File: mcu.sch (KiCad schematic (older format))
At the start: 95 parts, among them J1 USB_B_Mini, J10 JTAG, J2 SPI1, J3 uSD, J4 I2C1, J5 serial1, J6 serial2, J9 EXT_IOS, SW1 reset, U1 LP38691SD-3.3, U2 USBLC6-2SC6, U3 AT25SF641, U4 BQ24190, U5 STM32F750Z8, Y1 25 MHz, Y2 32.768 kHz

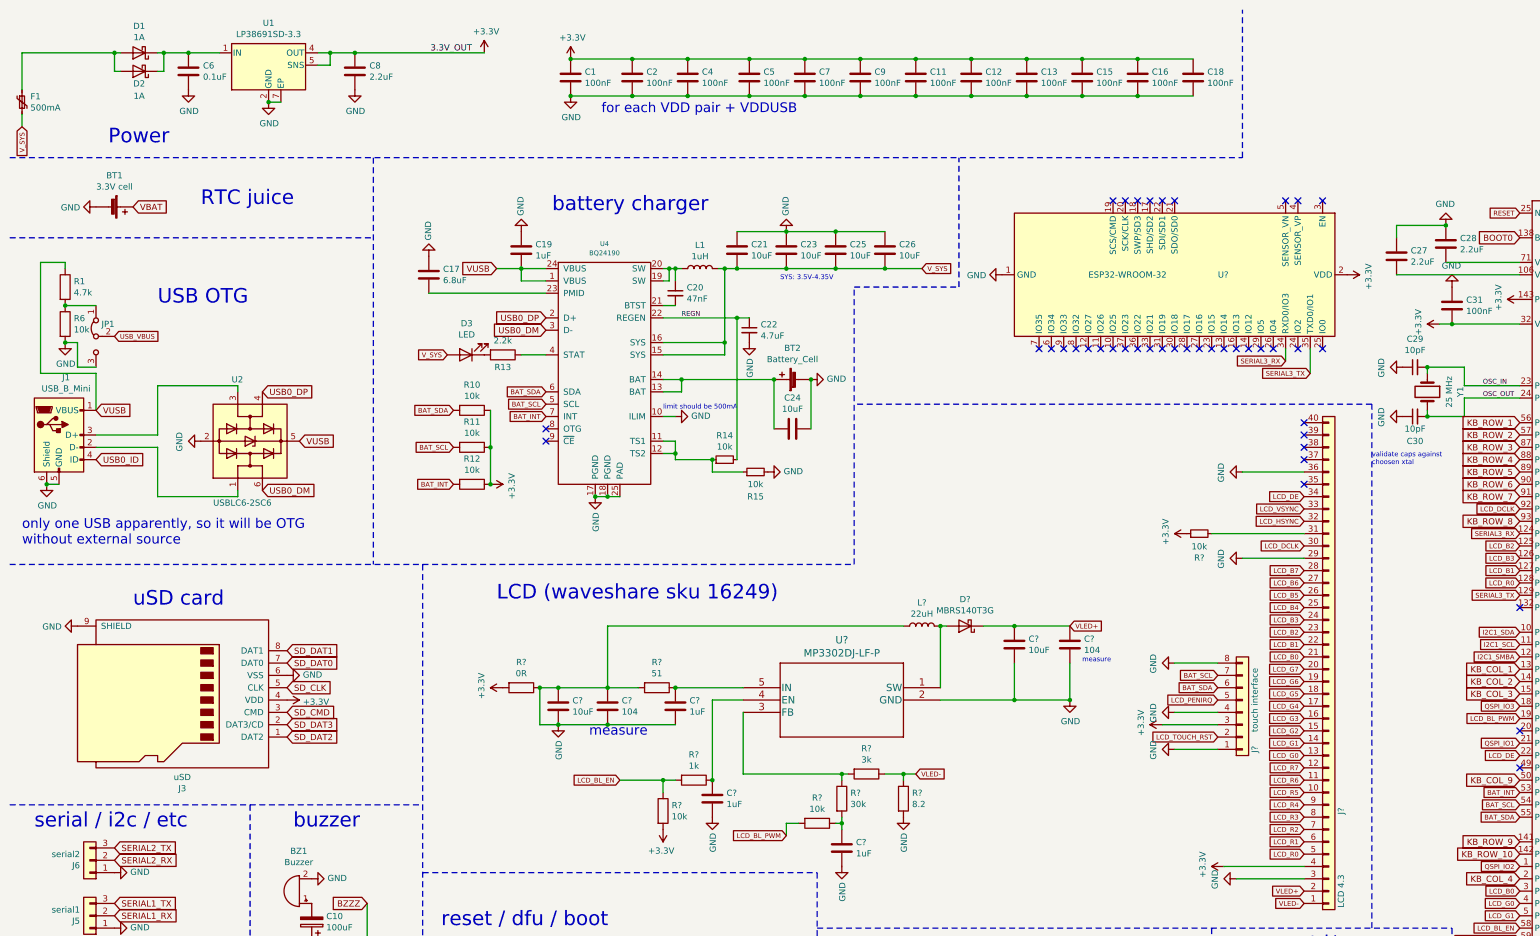
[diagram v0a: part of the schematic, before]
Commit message: Added some test points
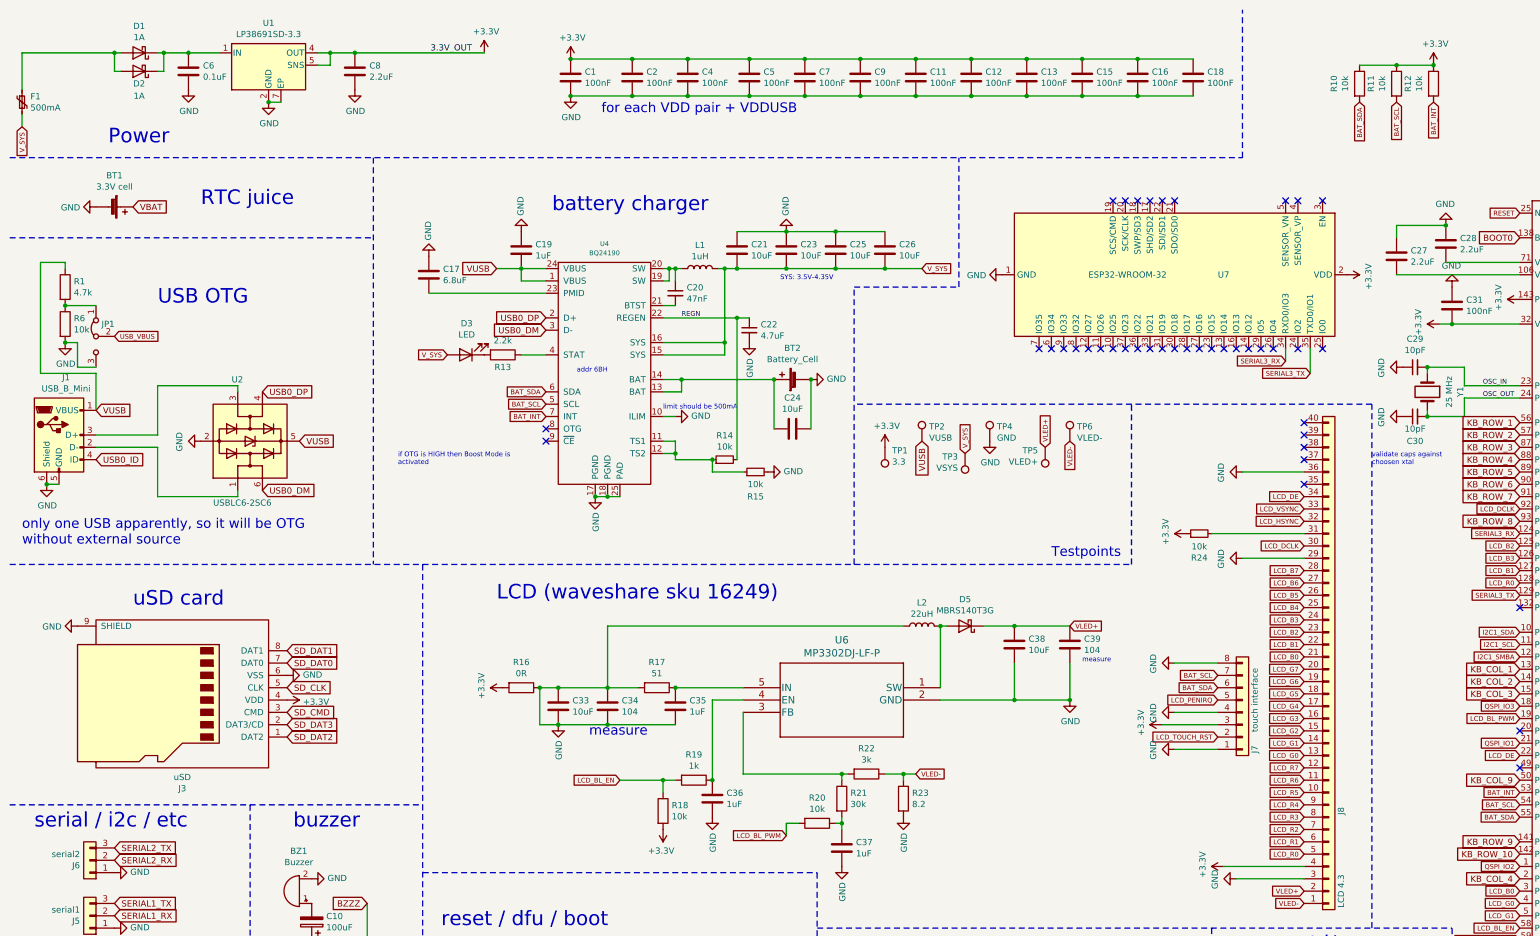
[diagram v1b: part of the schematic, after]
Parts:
- added TP1: 3.3, symbol Connector:TestPoint
- added TP2: VUSB, symbol Connector:TestPoint
- added TP3: VSYS, symbol Connector:TestPoint
- added TP4: GND, symbol Connector:TestPoint
- added TP5: VLED+, symbol Connector:TestPoint
- added TP6: VLED-, symbol Connector:TestPoint
- gave numbers to parts that had none: 22
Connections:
- net +3V3: now also TP1.1
- net GND: now also TP4.1
- net VLED+: now also TP5.1
- net VLED-: now also TP6.1
- net VUSB: now also TP2.1
- net V_SYS: now also TP3.1
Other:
- note added: "Testpoints"
- note added: "addr 6BH"
- note added: "if OTG is HIGH then Boost Mode is\nactivated"
- moved on the sheet: R10, R11, R12

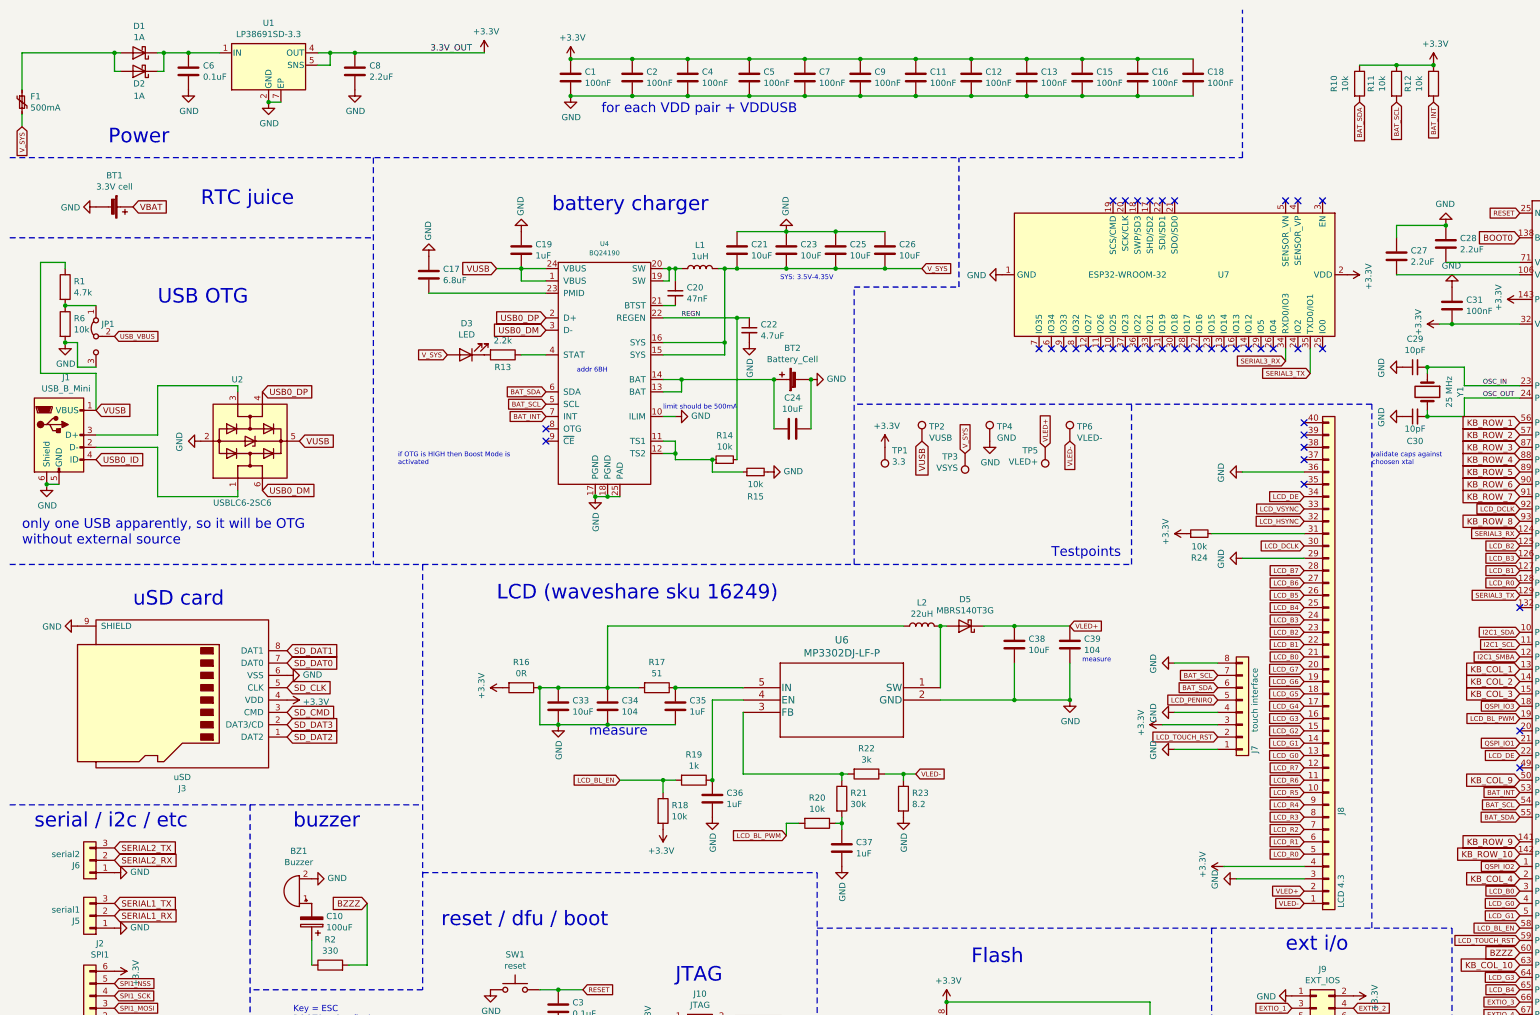
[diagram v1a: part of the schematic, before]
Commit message: Add a datasheet; Split power into own schematic
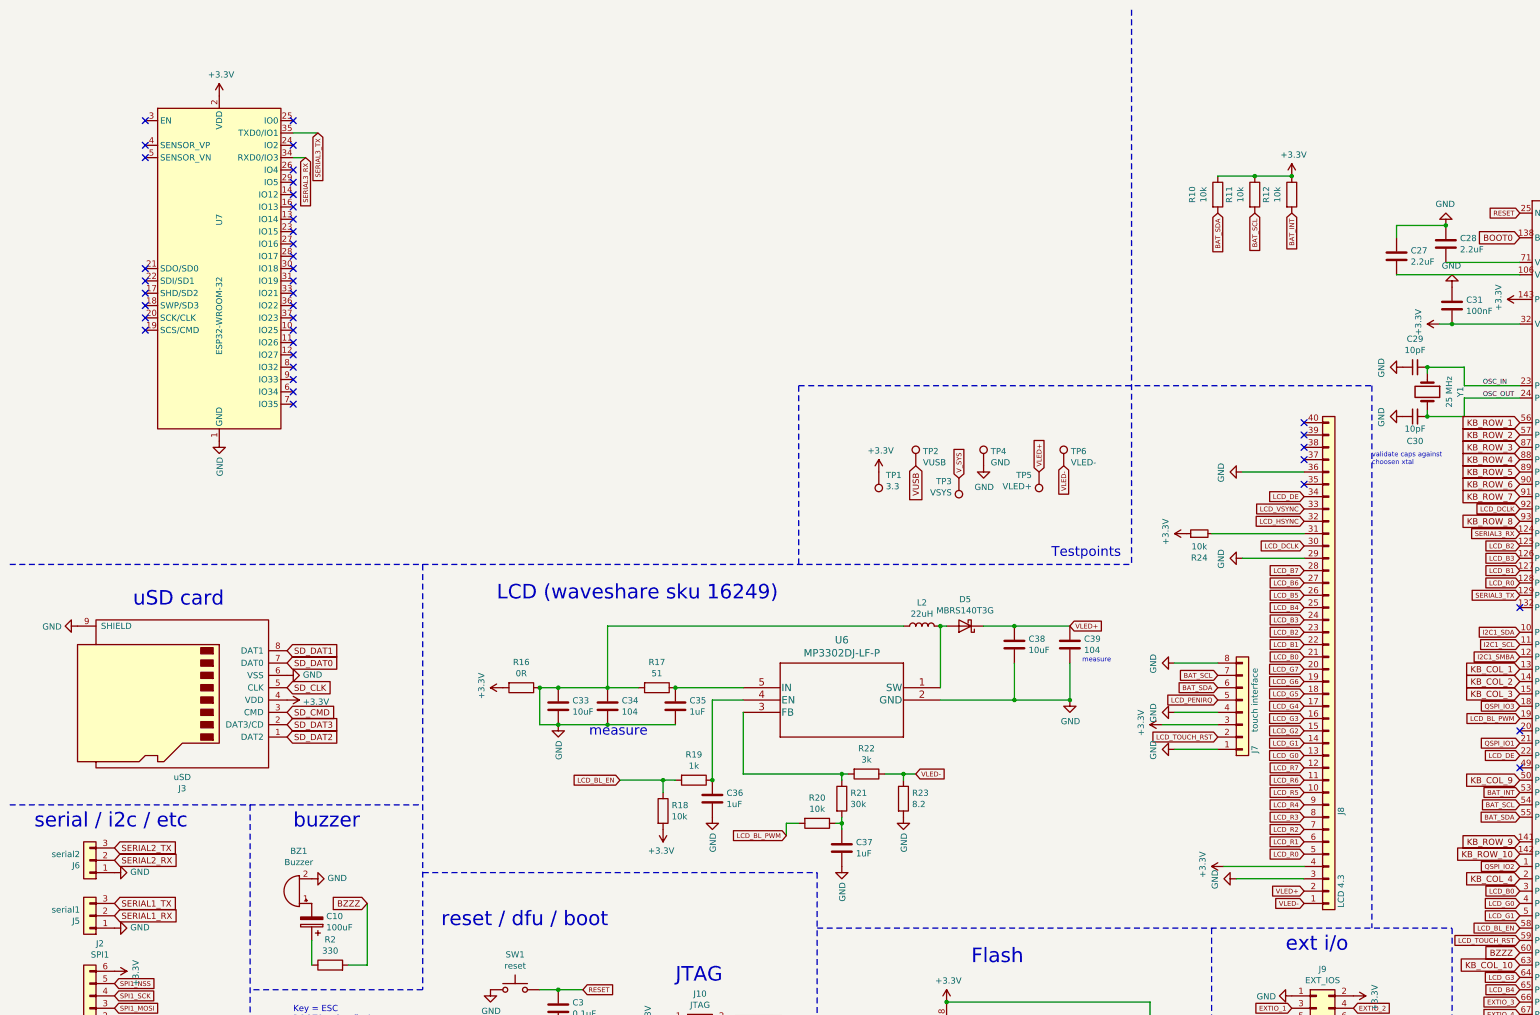
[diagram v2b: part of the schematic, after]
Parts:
- removed BT1: 3.3V cell, symbol Device:Battery_Cell
- removed BT2: Battery_Cell, symbol Device:Battery_Cell
- removed C1, C11, C12, C13, C15, C16, C18, C2, C4, C5, C7, C9: 100nF, symbol Device:C
- removed C17: 6.8uF, symbol Device:C
- removed C19: 1uF, symbol Device:C
- removed C20: 47nF, symbol Device:C_Small
- removed C21, C23, C24, C25, C26: 10uF, symbol Device:C
- removed C22: 4.7uF, symbol Device:C_Small
- removed C6: 0.1uF, symbol Device:C
- removed C8: 2.2uF, symbol Device:C
- removed D1, D2: 1A, symbol Device:D_Schottky
- removed D3: LED, symbol Device:LED
- removed F1: 500mA, symbol Device:Polyfuse_Small
- removed J1: USB_B_Mini, symbol Connector:USB_B_Mini
- removed JP1: Jumper_3_Bridged12, symbol Jumper:Jumper_3_Bridged12
- removed L1: 1uH, symbol Device:L
- removed R1: 4.7k, symbol Device:R
- removed R13: 2.2k, symbol Device:R
- removed R14, R15: 10k, symbol Device:R_Small
- removed R6: 10k, symbol Device:R
- removed U1: LP38691SD-3.3, Package_QFP:LQFP-144_20x20mm_P0.5mm, symbol Regulator_Linear:LP38691SD-3.3
- removed U2: USBLC6-2SC6, Package_TO_SOT_SMD:SOT-23-6, symbol Power_Protection:USBLC6-2SC6
- removed U4: BQ24190, symbol d_ti:BQ24190
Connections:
- no-connect marks 48 -> 46
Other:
- note removed: "Power"
- note removed: "RTC juice"
- note removed: "SYS: 3.5V-4.35V"
- note removed: "USB OTG"
- note removed: "addr 6BH"
- note removed: "battery charger"
- note removed: "for each VDD pair + VDDUSB"
- note removed: "if OTG is HIGH then Boost Mode is\nactivated"
- note removed: "limit should be 500mA"
- note removed: "only one USB apparently, so it will be OTG\nwithout external source"
- moved on the sheet: R10, R11, R12, TP1, TP2, TP3, TP4, TP5, TP6, U7

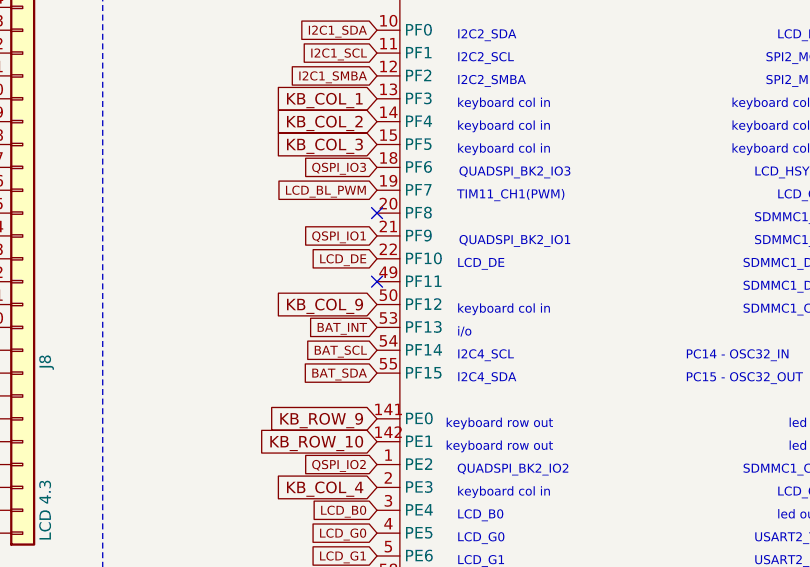
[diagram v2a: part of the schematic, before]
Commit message: Wire the OTG pin
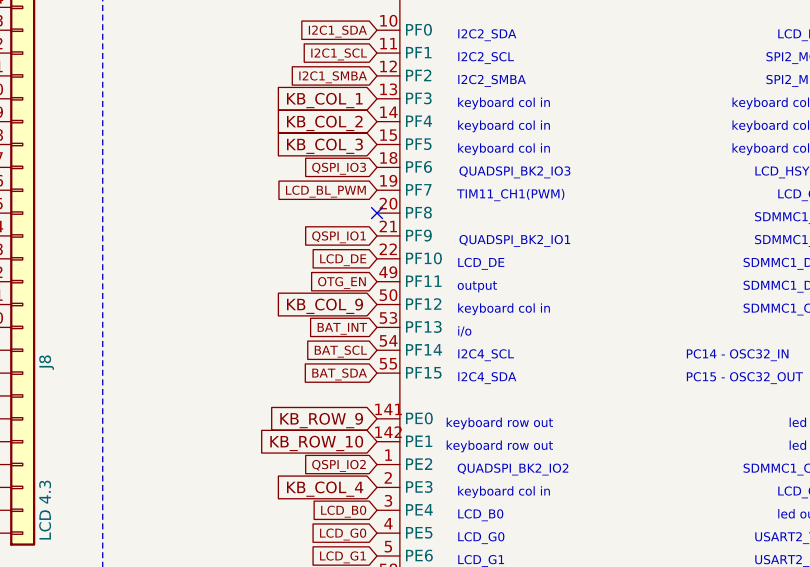
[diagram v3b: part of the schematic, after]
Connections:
- net OTG_EN: now reaches U5.49 (PF11)
- no-connect marks 46 -> 45
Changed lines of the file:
@@
 $EndComp
 NoConn ~ 12750 6350
-NoConn ~ 12750 6650
 Text GLabel 10300 5900 0    39   Input ~ 0
 BAT_SCL
@@
 Wire Notes Line
 	6900 3550 11550 3550
+Text GLabel 12750 6650 0    39   Input ~ 0
+OTG_EN
+Text Notes 13100 6700 0    39   ~ 0
+output
 $EndSCHEMATC
